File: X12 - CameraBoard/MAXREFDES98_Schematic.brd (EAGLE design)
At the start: 78.9 x 25.4 mm, 24 parts, among them U1 MB110S-TP, U2 MB110S-TP, U3 MAX5969AETB+, U4 MAX17503ATP+

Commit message: Reconfigured Board Layout
Reconfigured Board Layout
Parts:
- moved SV2 60.1 mm to (69.7, 5.21)
- moved R4 48.5 mm to (4.06, 14.9), turned to 0 degrees
- moved U2 46.0 mm to (72.6, 14.6), turned to 180 degrees
- moved L2 43.3 mm to (18.4, 4.06)
- moved D1 37.8 mm to (65.0, 24.4), turned to 270 degrees
- moved U1 37.8 mm to (72.5, 19.4), flipped to the bottom
- moved R5 37.7 mm to (4.06, 17.7), turned to 180 degrees
- moved C6 37.6 mm to (4.06, 11.8), turned to 0 degrees
- moved R1 30.9 mm to (61.8, 10.8), turned to 270 degrees
- moved C1 27.5 mm to (53.1, 8.13), turned to 180 degrees
- moved C8 22.6 mm to (4.19, 20.6), turned to 0 degrees
- moved C10 18.9 mm to (38.7, 18.9), turned to 180 degrees
- moved U4 18.8 mm to (18.0, 19.6)
- moved C4 18.5 mm to (38.7, 22.7), turned to 180 degrees
- moved R6 17.7 mm to (10.9, 17.1), flipped to the top, turned to 0 degrees
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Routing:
- net LX: track 47.2 -> 0.00 mm, vias 1 -> 0
- net GND: track 31.9 -> 0.00 mm, vias 2 -> 0
- net SV1_1/2: track 31.4 -> 0.00 mm, vias 3 -> 0
- net CLS: track 18.1 -> 0.00 mm
- net VSS_EP: track 10.8 -> 0.00 mm, vias 1 -> 0
- net BST: track 9.77 -> 0.00 mm
- net VDD: track 8.15 -> 0.00 mm
- net DET: track 5.94 -> 0.00 mm

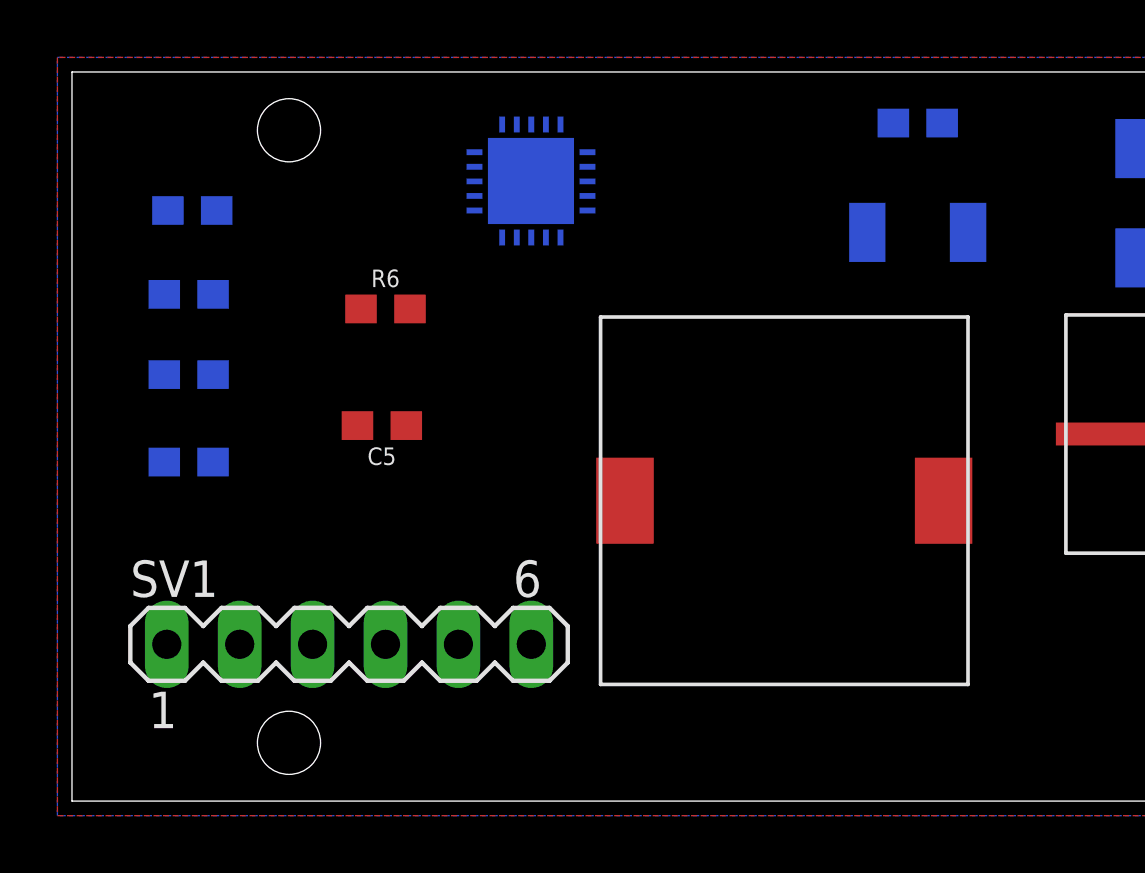
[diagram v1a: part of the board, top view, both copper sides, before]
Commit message: Update MAXREFDES98_Schematic.brd
rerouting
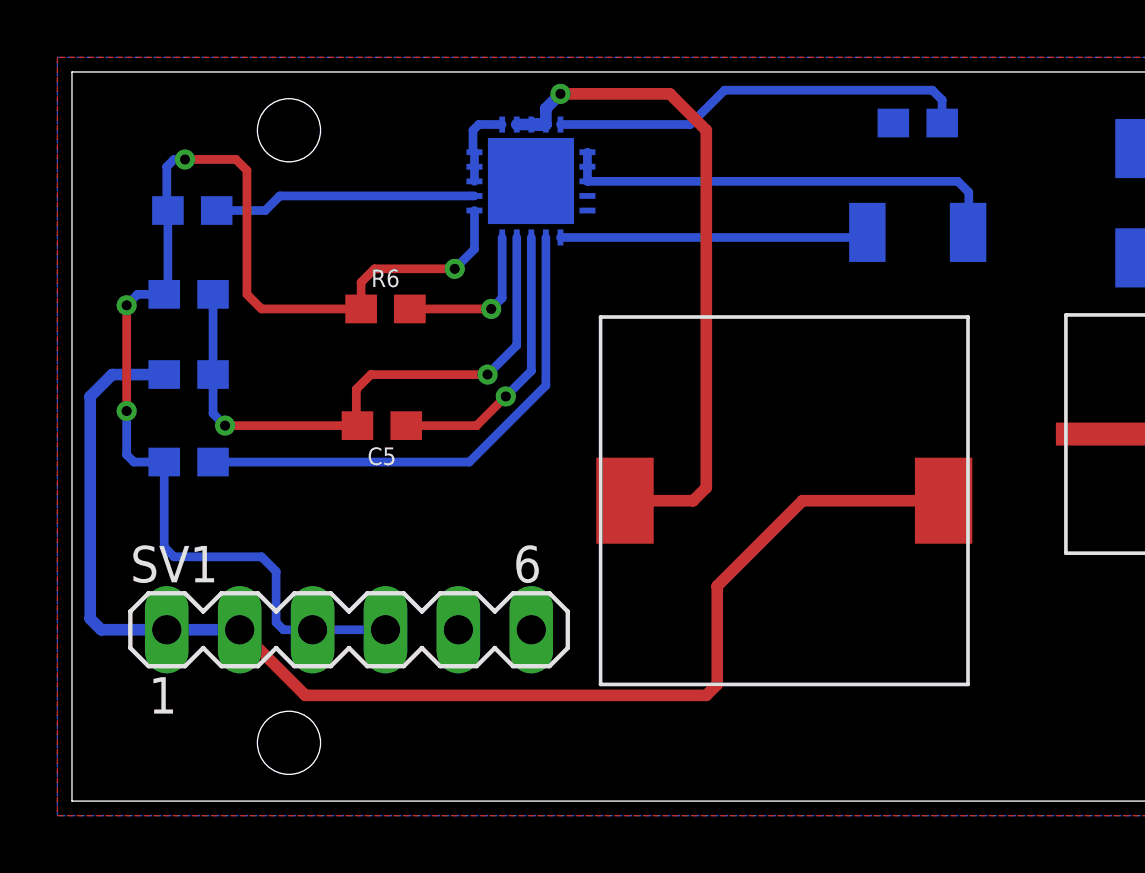
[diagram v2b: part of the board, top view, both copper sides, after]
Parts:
- moved SV1 0.51 mm to (9.65, 5.97)
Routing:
- net GND: track 0.00 -> 57.4 mm, vias 0 -> 4
- net SV1_1/2: track 0.00 -> 46.3 mm
- net LX: track 0.00 -> 24.4 mm, vias 0 -> 1
- net FB: track 0.00 -> 20.6 mm, vias 0 -> 2
- net SS: track 0.00 -> 17.9 mm
- net VIN: track 0.00 -> 15.9 mm
- net BST: track 0.00 -> 14.7 mm
- net CF: track 0.00 -> 9.79 mm, vias 0 -> 1
- net VCC: track 0.00 -> 9.19 mm
- net RT: track 0.00 -> 5.48 mm, vias 0 -> 1

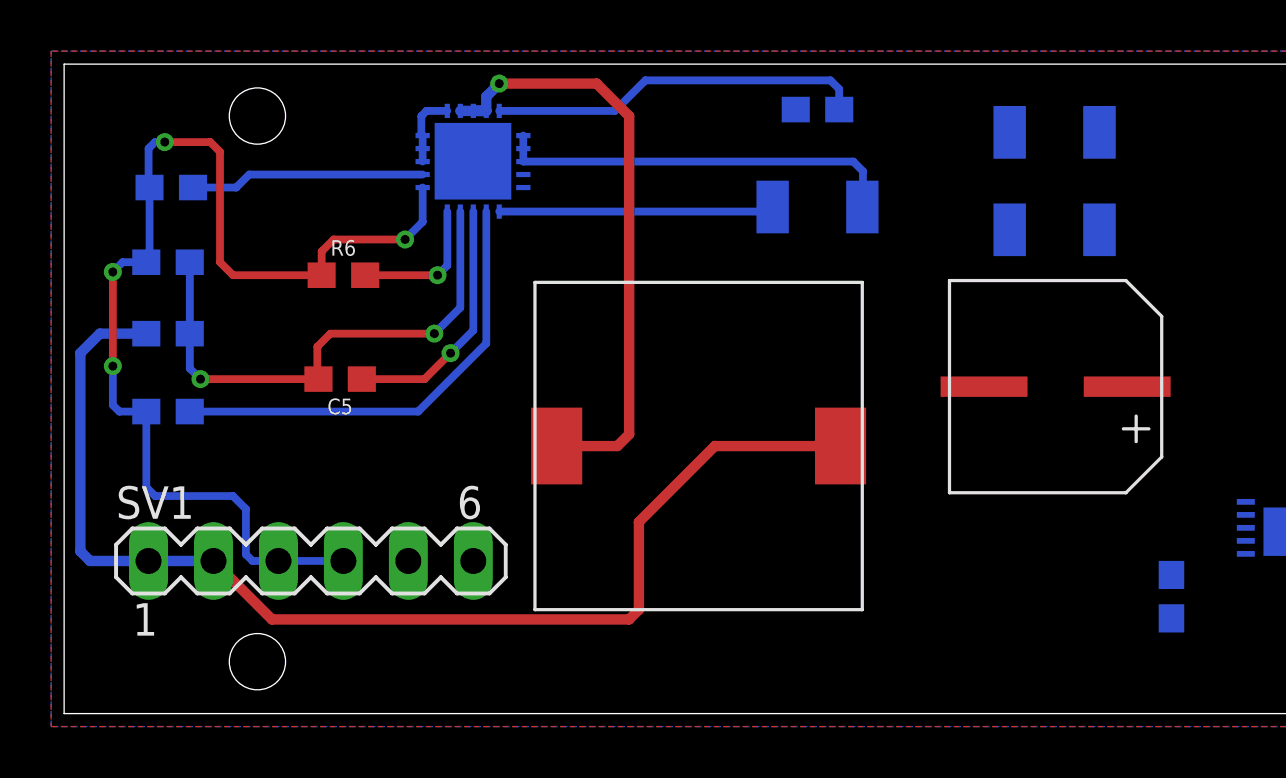
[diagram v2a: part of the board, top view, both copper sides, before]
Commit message: Update MAXREFDES98_Schematic.brd
routing
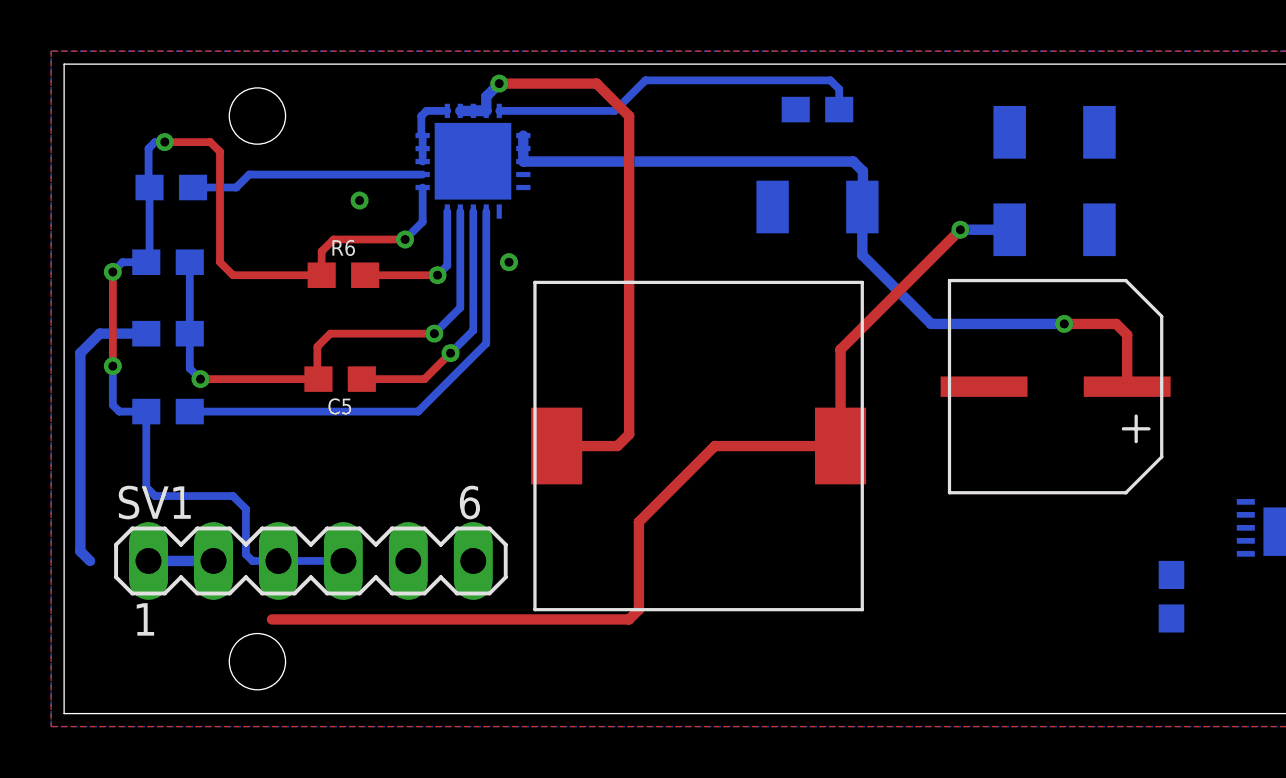
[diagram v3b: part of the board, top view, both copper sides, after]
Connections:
- net SV1_1/2 renamed 5V_OUT
- net SV2_1 renamed RECT_A_INPUT_1
- net SV2_2 renamed RECT_A_INPUT_2
- net SV2_3 renamed RECT_B_INPUT_1
- net SV2_4 renamed RECT_B_INPUT_2
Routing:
- net VIN: track 15.9 -> 31.4 mm, vias 0 -> 1
- net GND: track 57.4 -> 46.9 mm, vias 4 -> 5
- net 5V_OUT: track 46.3 -> 53.1 mm, vias 0 -> 1

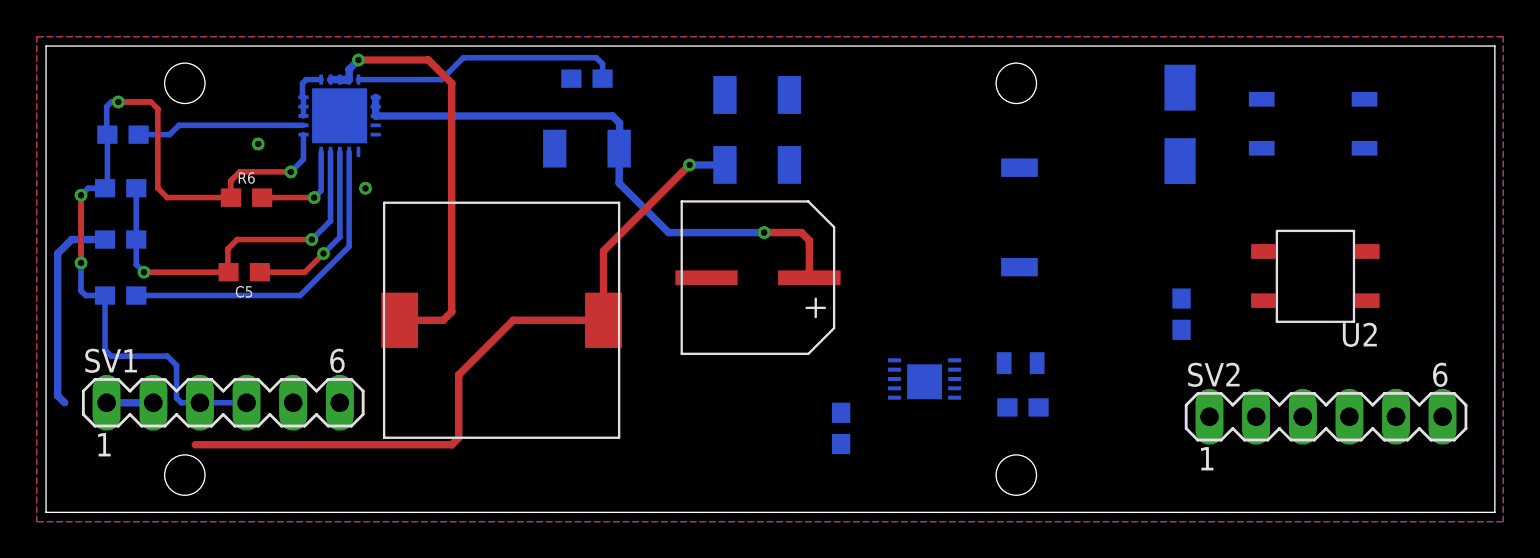
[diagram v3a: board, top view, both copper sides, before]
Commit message: Update MAXREFDES98_Schematic.brd
I know there are spacing issues with some traces, but I have not figured out how wide they need to be; so, I have made them larger than I think they need to be, for now.
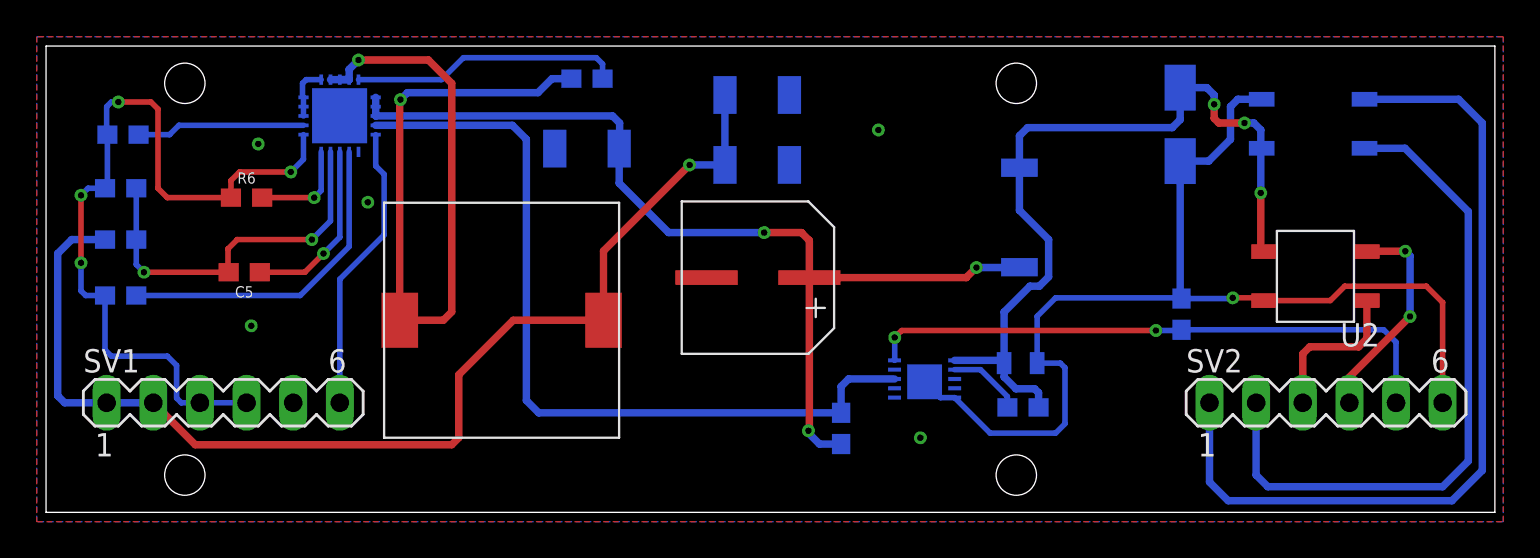
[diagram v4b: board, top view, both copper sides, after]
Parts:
- moved SV2 0.76 mm to (69.7, 5.97)
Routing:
- net VSS_EP: track 0.00 -> 59.3 mm, vias 0 -> 1
- net RECT_A_INPUT_1: track 0.00 -> 46.2 mm
- net PG_EN/UVLO: track 0.00 -> 44.7 mm
- net VDD: track 0.00 -> 44.7 mm, vias 0 -> 3
- net RECT_A_INPUT_2: track 0.00 -> 37.0 mm
- net CLS: track 0.00 -> 32.3 mm, vias 0 -> 2
- net VIN: track 31.4 -> 53.6 mm, vias 1 -> 3
- net LX: track 24.4 -> 45.7 mm, vias 1 -> 2
- net RESET: track 0.00 -> 15.8 mm
- net RECT_B_INPUT_2: track 0.00 -> 11.8 mm, vias 0 -> 2
- net 5V_OUT: track 53.1 -> 62.4 mm
- net RECT_B_INPUT_1: track 0.00 -> 8.57 mm
- net DET: track 0.00 -> 4.07 mm
- net GND: vias 5 -> 9

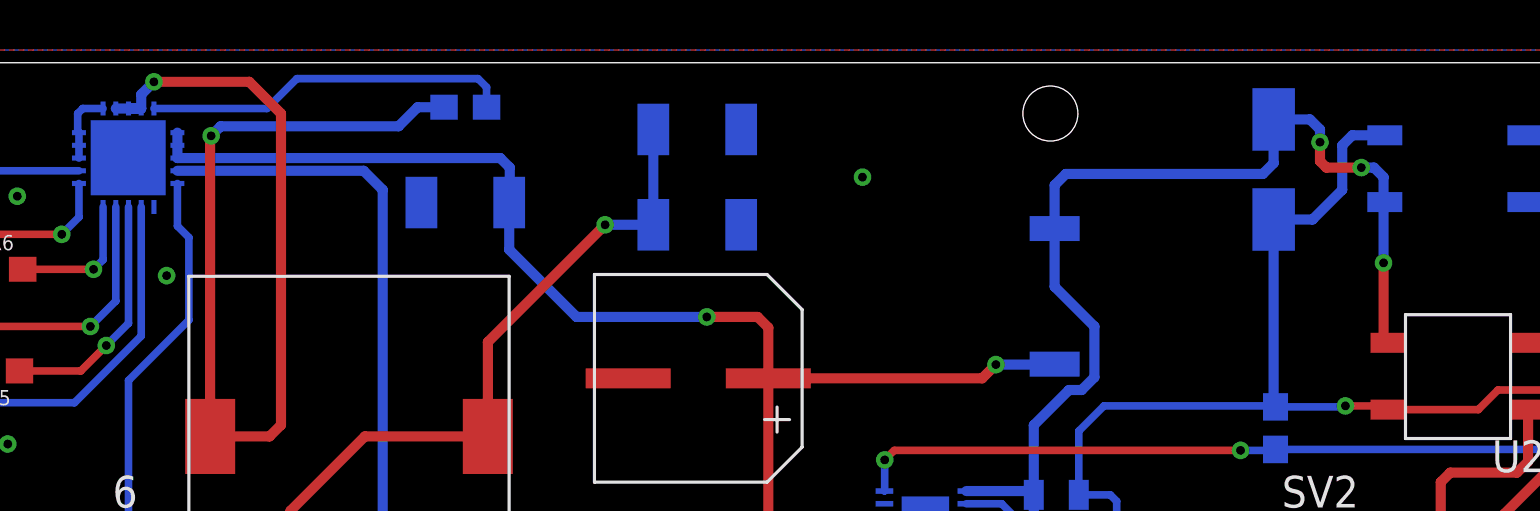
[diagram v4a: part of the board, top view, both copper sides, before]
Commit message: Update MAXREFDES98_Schematic.brd
fixed wire stub issues
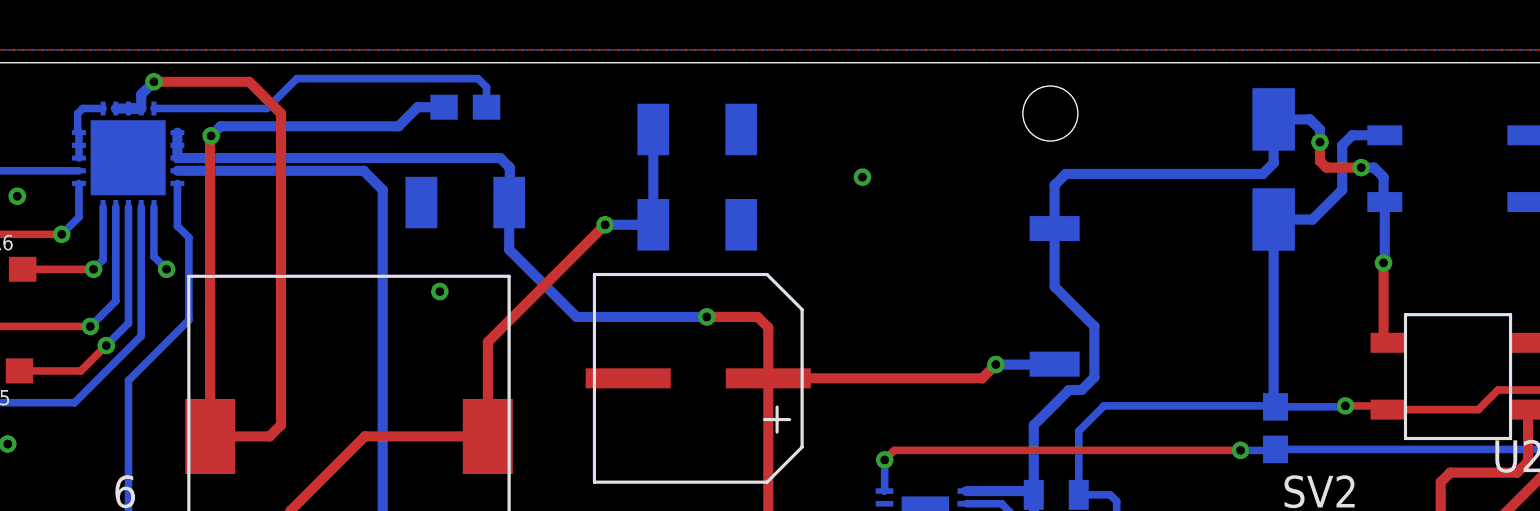
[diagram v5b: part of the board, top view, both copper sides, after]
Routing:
- net GND: track 46.9 -> 49.4 mm, vias 9 -> 10
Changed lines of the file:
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@@
 <wire x1="66.167" y1="14.382" x2="66.167" y2="17.399" width="0.4064" layer="1"/>
 <via x="66.167" y="17.399" extent="1-16" drill="0.35"/>
-<wire x1="66.167" y1="17.399" x2="66.167" y2="19.781" width="0.4064" layer="16"/>
 <wire x1="66.167" y1="19.781" x2="66.217" y2="19.831" width="0.4064" layer="16"/>
-<wire x1="66.217" y1="19.831" x2="66.167" y2="19.881" width="0.4064" layer="16"/>
 <wire x1="61.774" y1="23.134" x2="63.226" y2="23.134" width="0.4064" layer="16"/>
 <wire x1="63.226" y1="23.134" x2="63.627" y2="22.733" width="0.4064" layer="16"/>
@@
 <wire x1="65.786" y1="21.209" x2="66.167" y2="20.828" width="0.4064" layer="16"/>
 <wire x1="66.167" y1="20.828" x2="66.167" y2="19.781" width="0.4064" layer="16"/>
+<wire x1="66.217" y1="19.831" x2="66.217" y2="17.449" width="0.4064" layer="16"/>
+<wire x1="66.217" y1="17.449" x2="66.167" y2="17.399" width="0.4064" layer="16"/>
 </signal>
 <signal name="VSS_EP">
@@
 <wire x1="13.97" y1="23.368" x2="13.97" y2="22.6576" width="0.3048" layer="16"/>
 <wire x1="13.97" y1="22.6576" x2="14.0216" y2="22.606" width="0.3048" layer="16"/>
-<wire x1="27.5316" y1="19.6346" x2="27.709" y2="19.812" width="0.3048" layer="16"/>
 <wire x1="7.112" y1="6.223" x2="7.112" y2="8.001" width="0.3048" layer="16"/>
 <wire x1="6.604" y1="8.509" x2="7.112" y2="8.001" width="0.3048" layer="16"/>
@@
 <via x="11.176" y="10.16" extent="1-16" drill="0.35"/>
 <via x="45.339" y="20.828" extent="1-16" drill="0.35"/>
-<via x="17.526" y="16.891" extent="1-16" drill="0.35"/>
+<via x="17.526" y="17.145" extent="1-16" drill="0.35"/>
+<via x="28.448" y="16.256" extent="1-16" drill="0.35"/>
+<wire x1="17.018" y1="19.6346" x2="17.018" y2="17.653" width="0.3048" layer="16"/>
+<wire x1="17.018" y1="17.653" x2="17.526" y2="17.145" width="0.3048" layer="16"/>
 </signal>
 <signal name="RESET">

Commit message: Update MAXREFDES98_Schematic.brd
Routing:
- net PG_EN/UVLO: track 44.7 -> 43.7 mm
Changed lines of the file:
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@@
 <contactref element="R3" pad="1"/>
 <contactref element="U4" pad="EN/UVLO"/>
-<wire x1="17.9574" y1="21.082" x2="25.4" y2="21.082" width="0.4064" layer="16"/>
-<wire x1="25.4" y1="21.082" x2="26.162" y2="20.32" width="0.4064" layer="16"/>
 <wire x1="26.836" y1="5.422" x2="43.307" y2="5.422" width="0.4064" layer="16"/>
-<wire x1="26.162" y1="20.32" x2="26.162" y2="6.096" width="0.4064" layer="16"/>
 <wire x1="26.162" y1="6.096" x2="26.836" y2="5.422" width="0.4064" layer="16"/>
 <wire x1="46.216" y1="7.2645" x2="43.7135" y2="7.2645" width="0.4064" layer="16"/>
 <wire x1="43.7135" y1="7.2645" x2="43.307" y2="6.858" width="0.4064" layer="16"/>
 <wire x1="43.307" y1="6.858" x2="43.307" y2="5.422" width="0.4064" layer="16"/>
+<wire x1="17.9574" y1="21.082" x2="19.558" y2="21.082" width="0.4064" layer="16"/>
+<wire x1="20.32" y1="20.32" x2="24.511" y2="20.32" width="0.4064" layer="16"/>
+<wire x1="19.558" y1="21.082" x2="20.32" y2="20.32" width="0.4064" layer="16"/>
+<wire x1="24.511" y1="20.32" x2="26.162" y2="18.669" width="0.4064" layer="16"/>
+<wire x1="26.162" y1="18.669" x2="26.162" y2="6.096" width="0.4064" layer="16"/>
 </signal>
 <signal name="VIN">
